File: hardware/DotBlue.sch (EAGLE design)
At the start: 11 parts, among them IC1 CP2101, J3 USB-MICROB, U1 RFD77101, X3 S4B-ZR

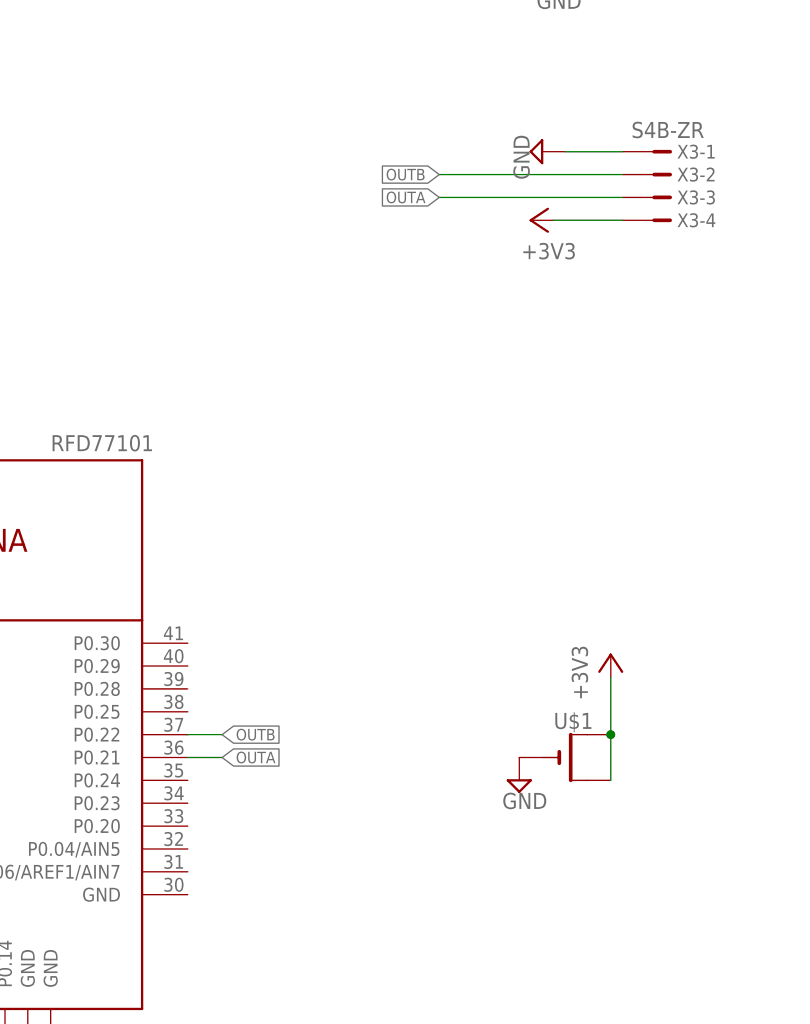
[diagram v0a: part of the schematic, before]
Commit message: Flip JST, add AIN
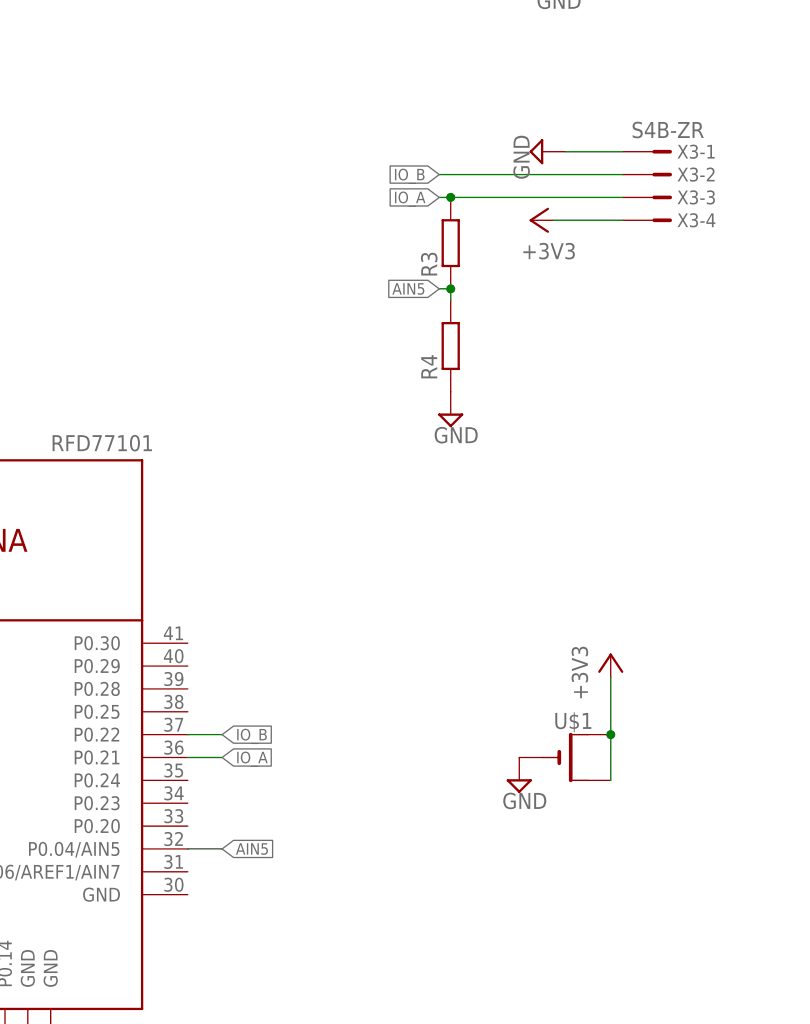
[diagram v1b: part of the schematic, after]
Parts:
- added R3, R4: (no value), rcl:R-EU_R0603
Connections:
- net OUTB renamed IO_B
- removed net OUTA: U1.P0.21, X3-3.1
- new net AIN5: R3.1, R4.2, U1.P0.04/AIN5
- new net IO_A: R3.2, U1.P0.21, X3-3.1
- net GND: now also R4.1
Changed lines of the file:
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@@
 <part name="C3" library="rcl" deviceset="C-EU" device="C0603" value="1uF"/>
 <part name="SUPPLY6" library="supply2" deviceset="GND" device=""/>
+<part name="R3" library="rcl" deviceset="R-EU_" device="R0603"/>
+<part name="R4" library="rcl" deviceset="R-EU_" device="R0603"/>
+<part name="SUPPLY8" library="supply2" deviceset="GND" device=""/>
 </parts>
 <sheets>
@@
 <instance part="C3" gate="G$1" x="21.59" y="170.18"/>
 <instance part="SUPPLY6" gate="GND" x="21.59" y="173.99" rot="R180"/>
+<instance part="R3" gate="G$1" x="118.11" y="107.95" rot="R90"/>
+<instance part="R4" gate="G$1" x="118.11" y="96.52" rot="R90"/>
+<instance part="SUPPLY8" gate="GND" x="118.11" y="88.9"/>
 </instances>
 <busses>
@@
 <wire x1="21.59" y1="172.72" x2="21.59" y2="171.45" width="0.1524" layer="91"/>
 </segment>
+<segment>
+<pinref part="R4" gate="G$1" pin="1"/>
+<pinref part="SUPPLY8" gate="GND" pin="GND"/>
+</segment>
 </net>
 <net name="+5V" class="0">
@@
 </segment>
 </net>
-<net name="OUTB" class="0">
-<segment>
-<label x="116.84" y="115.57" size="1.27" layer="95" rot="R180" xref="yes"/>
-<wire x1="137.16" y1="115.57" x2="116.84" y2="115.57" width="0.1524" layer="91"/>
-<pinref part="X3" gate="-2" pin="1"/>
-</segment>
-<segment>
-<pinref part="U1" gate="G$1" pin="P0.22"/>
-<wire x1="88.9" y1="53.34" x2="92.71" y2="53.34" width="0.1524" layer="91"/>
-<label x="92.71" y="53.34" size="1.27" layer="95" xref="yes"/>
-</segment>
-</net>
-<net name="OUTA" class="0">
-<segment>
-<pinref part="X3" gate="-3" pin="1"/>
-<wire x1="137.16" y1="113.03" x2="116.84" y2="113.03" width="0.1524" layer="91"/>
-<label x="116.84" y="113.03" size="1.27" layer="95" rot="R180" xref="yes"/>
-</segment>
-<segment>
-<pinref part="U1" gate="G$1" pin="P0.21"/>
-<wire x1="88.9" y1="50.8" x2="92.71" y2="50.8" width="0.1524" layer="91"/>
-<label x="92.71" y="50.8" size="1.27" layer="95" xref="yes"/>
-</segment>
-</net>
 <net name="LED_RED" class="0">
 <segment>
@@
 </segment>
 </net>
+<net name="IO_B" class="0">
+<segment>
+<pinref part="U1" gate="G$1" pin="P0.22"/>
+<wire x1="88.9" y1="53.34" x2="92.71" y2="53.34" width="0.1524" layer="91"/>
+<label x="92.71" y="53.34" size="1.27" layer="95" xref="yes"/>
+</segment>
+<segment>
+<label x="116.84" y="115.57" size="1.27" layer="95" rot="R180" xref="yes"/>
+<wire x1="137.16" y1="115.57" x2="116.84" y2="115.57" width="0.1524" layer="91"/>
+<pinref part="X3" gate="-2" pin="1"/>
+</segment>
+</net>
+<net name="IO_A" class="0">
+<segment>
+<pinref part="U1" gate="G$1" pin="P0.21"/>
+<wire x1="88.9" y1="50.8" x2="92.71" y2="50.8" width="0.1524" layer="91"/>
+<label x="92.71" y="50.8" size="1.27" layer="95" xref="yes"/>
+</segment>
+<segment>
+<pinref part="X3" gate="-3" pin="1"/>
+<wire x1="137.16" y1="113.03" x2="118.11" y2="113.03" width="0.1524" layer="91"/>
+<label x="116.84" y="113.03" size="1.27" layer="95" rot="R180" xref="yes"/>
+<pinref part="R3" gate="G$1" pin="2"/>
+<wire x1="118.11" y1="113.03" x2="116.84" y2="113.03" width="0.1524" layer="91"/>
+<junction x="118.11" y="113.03"/>
+</segment>
+</net>
+<net name="AIN5" class="0">
+<segment>
+<pinref part="U1" gate="G$1" pin="P0.04/AIN5"/>
+<wire x1="88.9" y1="40.64" x2="92.71" y2="40.64" width="0.1524" layer="91"/>
+<label x="92.71" y="40.64" size="1.27" layer="95" xref="yes"/>
+</segment>
+<segment>
+<pinref part="R3" gate="G$1" pin="1"/>
+<pinref part="R4" gate="G$1" pin="2"/>
+<wire x1="118.11" y1="102.87" x2="118.11" y2="101.6" width="0.1524" layer="91"/>
+<wire x1="118.11" y1="102.87" x2="116.84" y2="102.87" width="0.1524" layer="91"/>
+<junction x="118.11" y="102.87"/>
+<label x="116.84" y="102.87" size="1.27" layer="95" rot="R180" xref="yes"/>
+</segment>
+</net>

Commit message: Swap IO_AB for I2C pins, correct traces near pins, solidify GND
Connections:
- removed net IO_A: R3.2, U1.P0.21, X3-3.1
- removed net IO_B: U1.P0.22, X3-2.1
- new net SCL: U1.P0.05/AIN6, X3-2.1
- new net SDA: R3.2, U1.P0.06/AREF1/AIN7, X3-3.1
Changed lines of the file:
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@@
 </segment>
 </net>
-<net name="IO_B" class="0">
-<segment>
-<pinref part="U1" gate="G$1" pin="P0.22"/>
-<wire x1="88.9" y1="53.34" x2="92.71" y2="53.34" width="0.1524" layer="91"/>
-<label x="92.71" y="53.34" size="1.27" layer="95" xref="yes"/>
-</segment>
-<segment>
-<label x="116.84" y="115.57" size="1.27" layer="95" rot="R180" xref="yes"/>
-<wire x1="137.16" y1="115.57" x2="116.84" y2="115.57" width="0.1524" layer="91"/>
-<pinref part="X3" gate="-2" pin="1"/>
-</segment>
-</net>
-<net name="IO_A" class="0">
-<segment>
-<pinref part="U1" gate="G$1" pin="P0.21"/>
-<wire x1="88.9" y1="50.8" x2="92.71" y2="50.8" width="0.1524" layer="91"/>
-<label x="92.71" y="50.8" size="1.27" layer="95" xref="yes"/>
-</segment>
+<net name="SDA" class="0">
 <segment>
 <pinref part="X3" gate="-3" pin="1"/>
@@
 <wire x1="118.11" y1="113.03" x2="116.84" y2="113.03" width="0.1524" layer="91"/>
 <junction x="118.11" y="113.03"/>
+</segment>
+<segment>
+<pinref part="U1" gate="G$1" pin="P0.06/AREF1/AIN7"/>
+<wire x1="88.9" y1="38.1" x2="92.71" y2="38.1" width="0.1524" layer="91"/>
+<label x="92.71" y="38.1" size="1.27" layer="95" xref="yes"/>
 </segment>
 </net>
@@
 </segment>
 </net>
+<net name="SCL" class="0">
+<segment>
+<pinref part="U1" gate="G$1" pin="P0.05/AIN6"/>
+<wire x1="48.26" y1="17.78" x2="48.26" y2="15.24" width="0.1524" layer="91"/>
+<label x="48.26" y="15.24" size="1.27" layer="95" rot="R270" xref="yes"/>
+</segment>
+<segment>
+<label x="116.84" y="115.57" size="1.27" layer="95" rot="R180" xref="yes"/>
+<wire x1="137.16" y1="115.57" x2="116.84" y2="115.57" width="0.1524" layer="91"/>
+<pinref part="X3" gate="-2" pin="1"/>
+</segment>
+</net>

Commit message: Allign passive components
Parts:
- added BTN1: SPST.B3U-1000P(M), omron:SPST.B3U-1000P(M)
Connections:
- new net N$3: BTN1.1, U1.P0.21
- net GND: now also BTN1.2
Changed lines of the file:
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@@
 <part name="R4" library="rcl" deviceset="R-EU_" device="R0603"/>
 <part name="SUPPLY8" library="supply2" deviceset="GND" device=""/>
+<part name="BTN1" library="omron" deviceset="SPST" device=".B3U-1000P(M)"/>
+<part name="SUPPLY9" library="supply2" deviceset="GND" device=""/>
 </parts>
 <sheets>
@@
 <instance part="R4" gate="G$1" x="118.11" y="96.52" rot="R90"/>
 <instance part="SUPPLY8" gate="GND" x="118.11" y="88.9"/>
+<instance part="BTN1" gate="G$1" x="96.52" y="50.8"/>
+<instance part="SUPPLY9" gate="GND" x="99.06" y="45.72"/>
 </instances>
 <busses>
@@
 <pinref part="SUPPLY8" gate="GND" pin="GND"/>
 </segment>
+<segment>
+<pinref part="BTN1" gate="G$1" pin="2"/>
+<pinref part="SUPPLY9" gate="GND" pin="GND"/>
+<wire x1="99.06" y1="50.8" x2="99.06" y2="48.26" width="0.1524" layer="91"/>
+</segment>
 </net>
 <net name="+5V" class="0">
@@
 </segment>
 </net>
+<net name="N$3" class="0">
+<segment>
+<pinref part="BTN1" gate="G$1" pin="1"/>
+<pinref part="U1" gate="G$1" pin="P0.21"/>
+<wire x1="93.98" y1="50.8" x2="88.9" y2="50.8" width="0.1524" layer="91"/>
+</segment>
+</net>

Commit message: Add 3-way JMP for 3V-5V switch of JST
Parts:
- added JP1: JUMPER-SMT_3_1-NC_TRACE_NO-SILK, SparkFun-Jumpers:JUMPER-SMT_3_1-NC_TRACE_NO-SILK
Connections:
- new net N$5: JP1.2, X3-4.1
- net +3V3: now also JP1.3; no longer X3-4.1
- net +5V: now also JP1.1
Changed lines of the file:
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@@
 <part name="BTN1" library="omron" deviceset="SPST" device=".B3U-1000P(M)"/>
 <part name="SUPPLY9" library="supply2" deviceset="GND" device=""/>
+<part name="P+1" library="supply1" deviceset="+5V" device=""/>
+<part name="JP1" library="SparkFun-Jumpers" deviceset="JUMPER-SMT_3_1-NC_TRACE" device="_NO-SILK"/>
 </parts>
 <sheets>
@@
 <instance part="SUPPLY3" gate="GND" x="71.12" y="12.7"/>
 <instance part="+3V2" gate="G$1" x="-22.86" y="66.04" rot="R90"/>
-<instance part="+3V3" gate="G$1" x="127" y="110.49" rot="R90"/>
+<instance part="+3V3" gate="G$1" x="127" y="97.79" rot="R180"/>
 <instance part="C1" gate="G$1" x="-13.97" y="63.5"/>
 <instance part="SUPPLY4" gate="GND" x="-13.97" y="55.88"/>
@@
 <instance part="BTN1" gate="G$1" x="96.52" y="50.8"/>
 <instance part="SUPPLY9" gate="GND" x="99.06" y="45.72"/>
+<instance part="P+1" gate="1" x="148.59" y="97.79" rot="R180"/>
+<instance part="JP1" gate="G$1" x="137.16" y="102.87" rot="R270"/>
 </instances>
 <busses>
@@
 <junction x="17.78" y="165.1"/>
 </segment>
+<segment>
+<pinref part="JP1" gate="G$1" pin="1"/>
+<pinref part="P+1" gate="1" pin="+5V"/>
+<wire x1="142.24" y1="102.87" x2="148.59" y2="102.87" width="0.1524" layer="91"/>
+<wire x1="148.59" y1="102.87" x2="148.59" y2="100.33" width="0.1524" layer="91"/>
+</segment>
 </net>
 <net name="USB_D-" class="0">
@@
 </segment>
 <segment>
-<pinref part="+3V3" gate="G$1" pin="+3V3"/>
-<pinref part="X3" gate="-4" pin="1"/>
-<wire x1="129.54" y1="110.49" x2="137.16" y2="110.49" width="0.1524" layer="91"/>
-</segment>
-<segment>
 <pinref part="+3V4" gate="G$1" pin="+3V3"/>
 <pinref part="U$1" gate="G$1" pin="+"/>
@@
 <wire x1="135.89" y1="53.34" x2="135.89" y2="48.26" width="0.1524" layer="91"/>
 <junction x="135.89" y="53.34"/>
+</segment>
+<segment>
+<pinref part="JP1" gate="G$1" pin="3"/>
+<pinref part="+3V3" gate="G$1" pin="+3V3"/>
+<wire x1="132.08" y1="102.87" x2="127" y2="102.87" width="0.1524" layer="91"/>
+<wire x1="127" y1="102.87" x2="127" y2="100.33" width="0.1524" layer="91"/>
 </segment>
 </net>
@@
 </segment>
 </net>
+<net name="N$5" class="0">
+<segment>
+<pinref part="X3" gate="-4" pin="1"/>
+<pinref part="JP1" gate="G$1" pin="2"/>
+<wire x1="137.16" y1="110.49" x2="137.16" y2="107.95" width="0.1524" layer="91"/>
+</segment>
+</net>

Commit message: Add RGB connections
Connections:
- net LED_BLUE: now also U1.P0.28
- net LED_GREEN: now also U1.P0.29
- net LED_RED: now also U1.P0.25
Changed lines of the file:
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@@
 <pinref part="R1" gate="D" pin="1"/>
+</segment>
+<segment>
+<pinref part="U1" gate="G$1" pin="P0.25"/>
+<wire x1="88.9" y1="55.88" x2="93.98" y2="55.88" width="0.1524" layer="91"/>
+<label x="93.98" y="55.88" size="1.27" layer="95" xref="yes"/>
 </segment>
 </net>
@@
 <pinref part="R1" gate="B" pin="1"/>
 </segment>
+<segment>
+<pinref part="U1" gate="G$1" pin="P0.29"/>
+<wire x1="88.9" y1="60.96" x2="93.98" y2="60.96" width="0.1524" layer="91"/>
+<label x="93.98" y="60.96" size="1.27" layer="95" xref="yes"/>
+</segment>
 </net>
 <net name="LED_BLUE" class="0">
@@
 <pinref part="R1" gate="C" pin="1"/>
 </segment>
+<segment>
+<pinref part="U1" gate="G$1" pin="P0.28"/>
+<wire x1="88.9" y1="58.42" x2="93.98" y2="58.42" width="0.1524" layer="91"/>
+<label x="93.98" y="58.42" size="1.27" layer="95" xref="yes"/>
+</segment>
 </net>

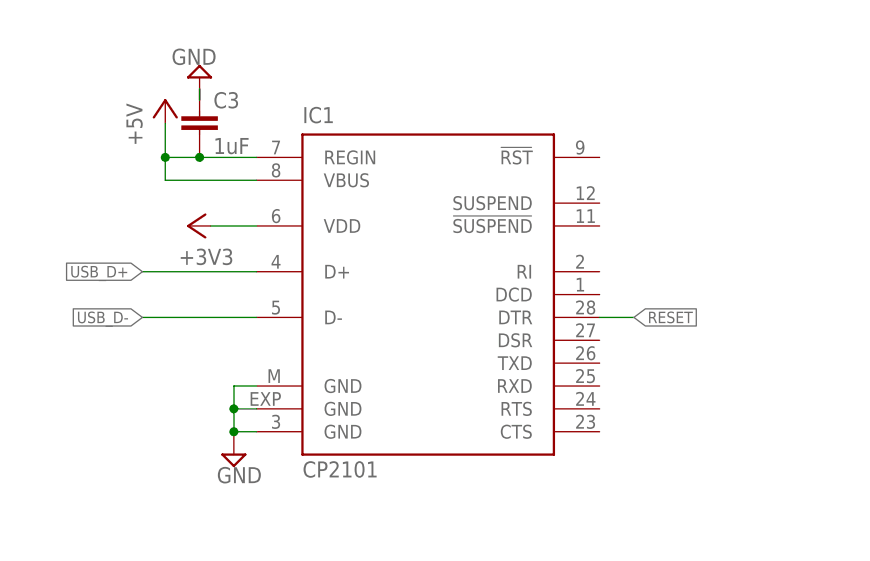
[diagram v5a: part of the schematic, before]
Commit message: Add UART connections
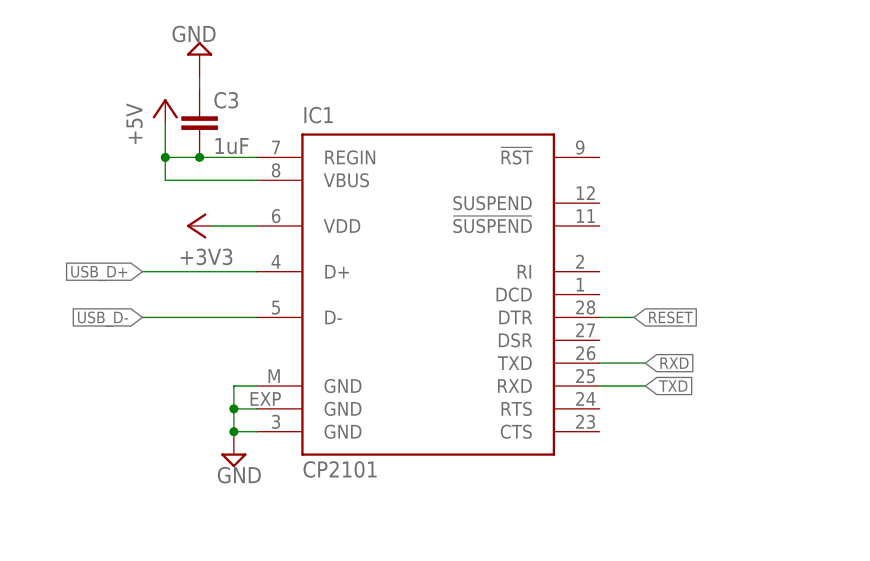
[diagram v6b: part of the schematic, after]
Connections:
- net RXD: now also IC1.TXD
- net TXD: now also IC1.RXD
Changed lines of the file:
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@@
 <setting verticaltext="up"/>
 </settings>
-<grid distance="0.05" unitdist="inch" unit="inch" style="lines" multiple="1" display="no" altdistance="0.01" altunitdist="inch" altunit="inch"/>
+<grid distance="0.1" unitdist="inch" unit="inch" style="lines" multiple="1" display="no" altdistance="0.01" altunitdist="inch" altunit="inch"/>
 <layers>
 <layer number="1" name="Top" color="4" fill="1" visible="no" active="no"/>
@@
 <instance part="SUPPLY5" gate="GND" x="125.73" y="48.26"/>
 <instance part="C3" gate="G$1" x="21.59" y="170.18"/>
-<instance part="SUPPLY6" gate="GND" x="21.59" y="173.99" rot="R180"/>
+<instance part="SUPPLY6" gate="GND" x="21.59" y="176.53" rot="R180"/>
 <instance part="R3" gate="G$1" x="118.11" y="107.95" rot="R90"/>
 <instance part="R4" gate="G$1" x="118.11" y="96.52" rot="R90"/>
@@
 <pinref part="C3" gate="G$1" pin="1"/>
 <pinref part="SUPPLY6" gate="GND" pin="GND"/>
-<wire x1="21.59" y1="172.72" x2="21.59" y2="171.45" width="0.1524" layer="91"/>
+<wire x1="21.59" y1="172.72" x2="21.59" y2="173.99" width="0.1524" layer="91"/>
 </segment>
 <segment>
@@
 <label x="53.34" y="15.24" size="1.27" layer="95" rot="R270" xref="yes"/>
 </segment>
+<segment>
+<pinref part="IC1" gate="G$1" pin="RXD"/>
+<wire x1="66.04" y1="139.7" x2="71.12" y2="139.7" width="0.1524" layer="91"/>
+<label x="71.12" y="139.7" size="1.27" layer="95" xref="yes"/>
+</segment>
 </net>
 <net name="RXD" class="0">
@@
 <wire x1="58.42" y1="17.78" x2="58.42" y2="15.24" width="0.1524" layer="91"/>
 <label x="58.42" y="15.24" size="1.27" layer="95" rot="R270" xref="yes"/>
+</segment>
+<segment>
+<pinref part="IC1" gate="G$1" pin="TXD"/>
+<wire x1="66.04" y1="142.24" x2="71.12" y2="142.24" width="0.1524" layer="91"/>
+<label x="71.12" y="142.24" size="1.27" layer="95" xref="yes"/>
 </segment>
 </net>
@@
 </sheet>
 </sheets>
+<errors>
+</errors>
 </schematic>
 </drawing>
